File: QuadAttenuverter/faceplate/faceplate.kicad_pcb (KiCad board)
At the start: 2 copper layers, 40.3 x 128.5 mm, 20 parts

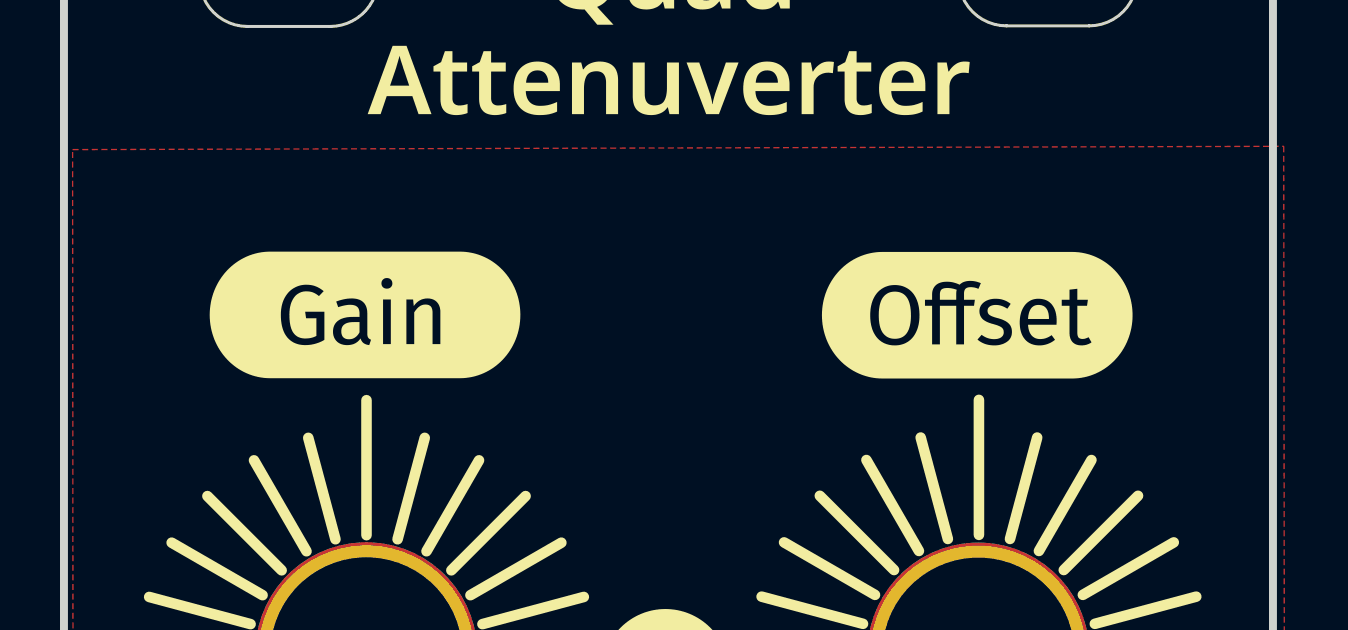
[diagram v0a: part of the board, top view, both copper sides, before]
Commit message: Add M3 mount for mechanical stability, and update power
If pots are used that don't have mounting brackets, the faceplate needs
extra mechanical support at the top. Two M3 screws can support that.

In addition, bottom silk screen is added for the power connector, since
it's probably going to be mounted there.
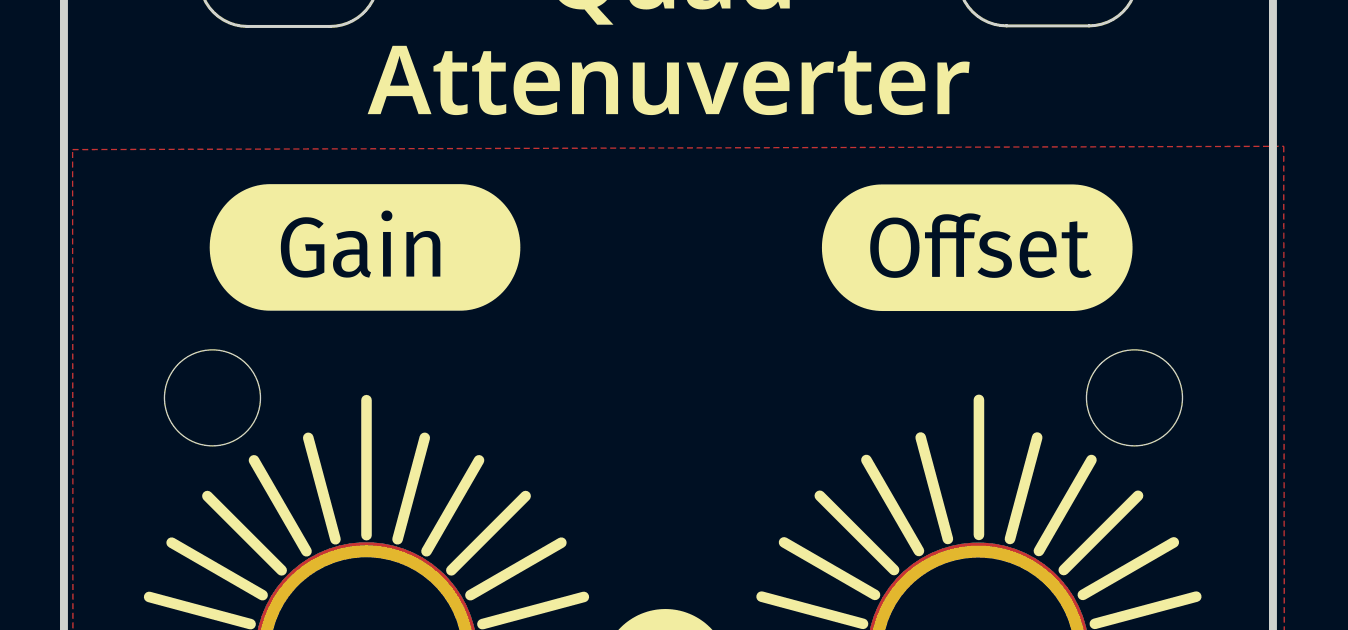
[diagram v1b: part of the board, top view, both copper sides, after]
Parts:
- added REF**: MountingHole_3.2mm_M3_NoCourt, Library:MountingHole_3.2mm_M3_NoCourt, F.Cu at (66.2, 57.0)
- added REF**: MountingHole_3.2mm_M3_NoCourt, Library:MountingHole_3.2mm_M3_NoCourt, F.Cu at (96.9, 57.0)
